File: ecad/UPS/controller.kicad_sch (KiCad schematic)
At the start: 32 parts, among them J2 Conn_01x05_Socket, SW1 SW_Push, SW2 SW_Push, U1 STM32L152RCT6, U2 AP2112K-3.3TRG1

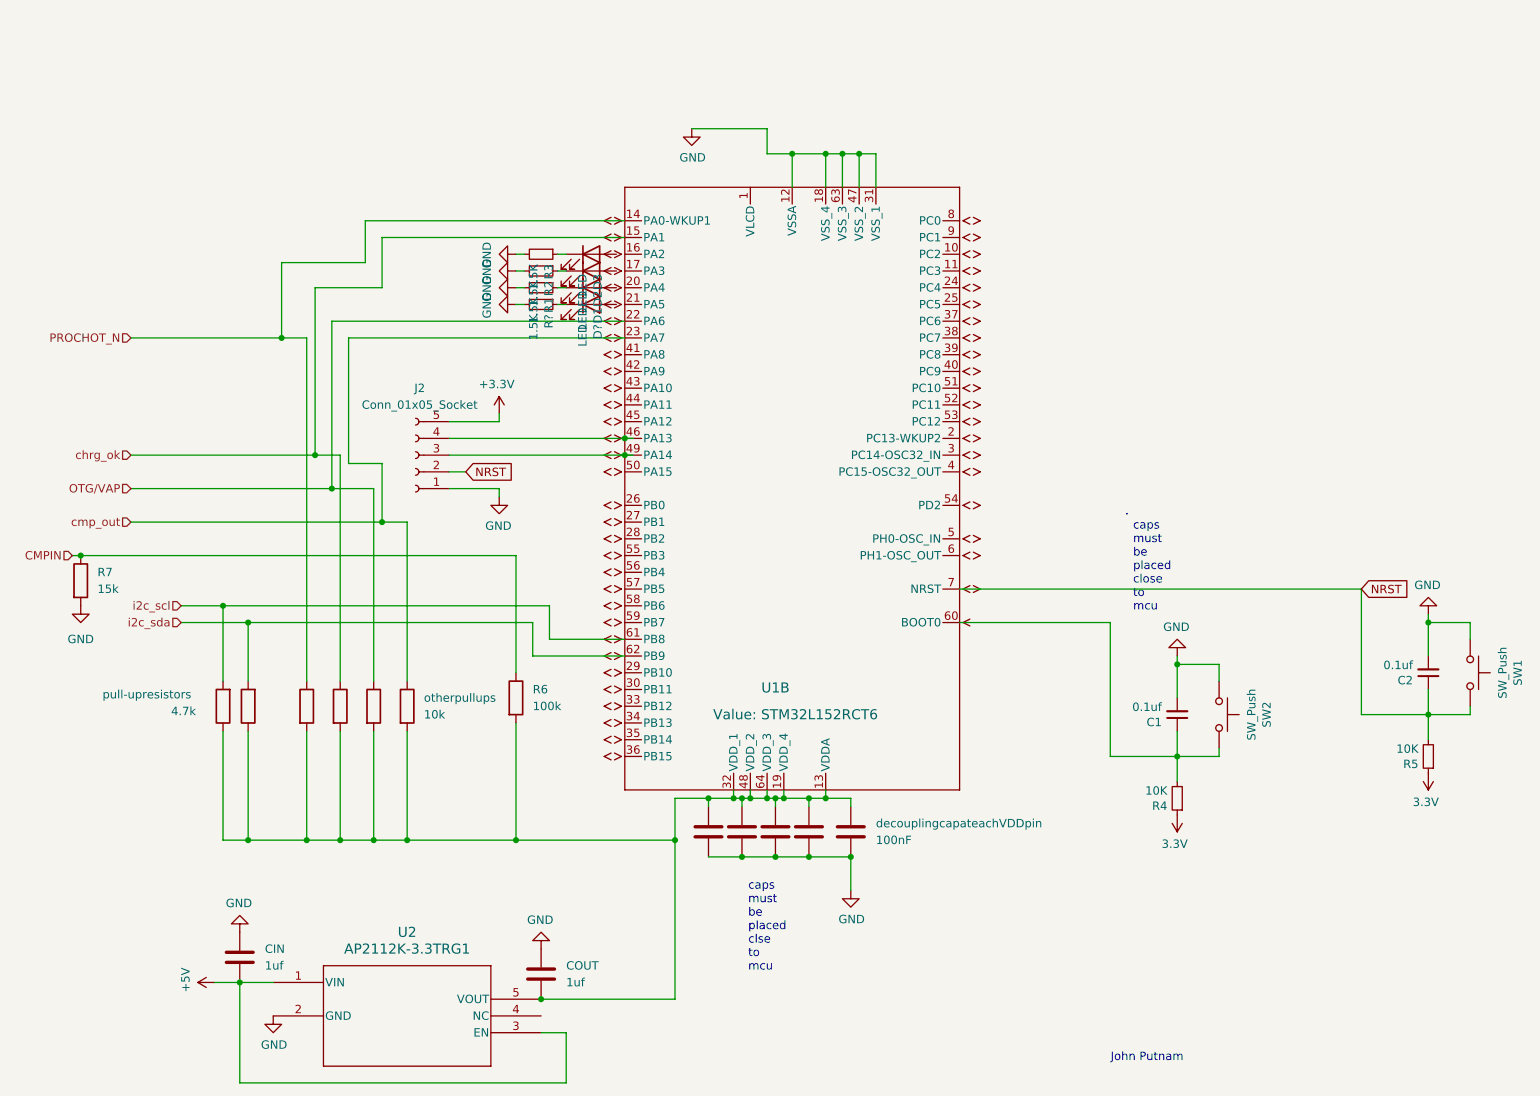
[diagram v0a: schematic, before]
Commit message: Made Power Net Class and set up board parameters and constraints
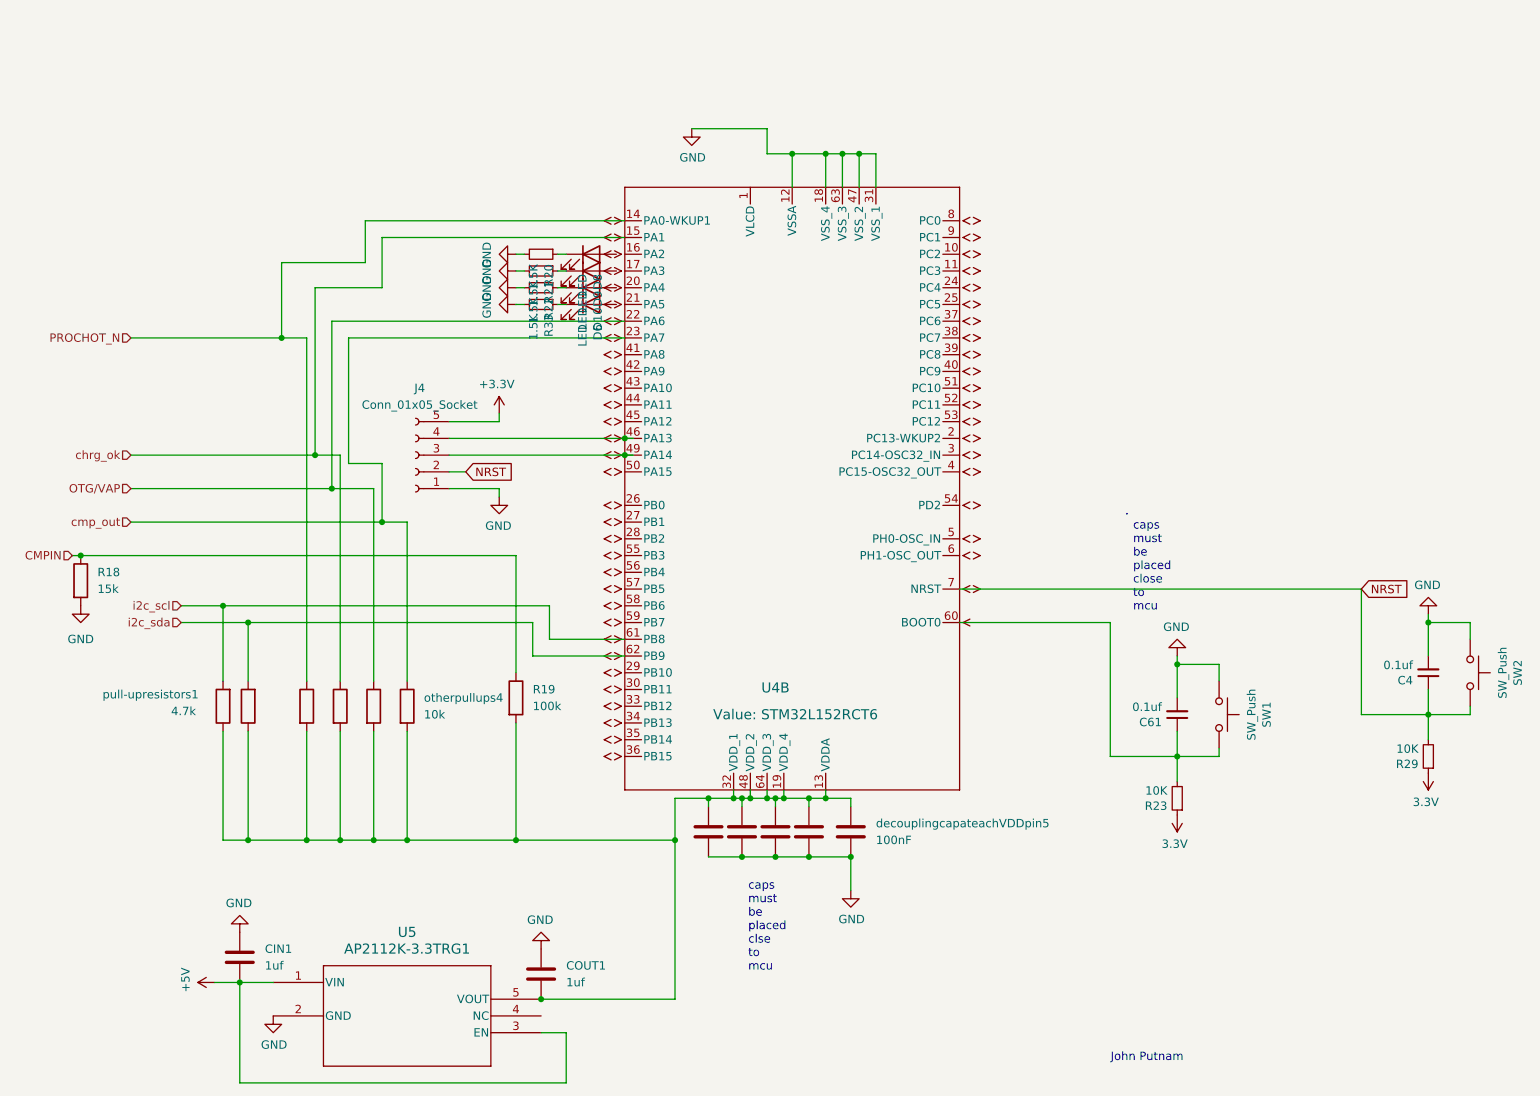
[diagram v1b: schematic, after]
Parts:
- gave numbers to parts that had none: 2
- renumbered C2 to C4, C1 to C61, CIN to CIN1, COUT to COUT1, D1 to D10, D3 to D8, D2 to D9, J2 to J4, R7 to R18, R6 to R19, R3 to R20, R2 to R21, R1 to R22, R4 to R23, R5 to R29, SW2 to SW1, SW1 to SW2, U1 to U4, U2 to U5, decouplingcapateachVDDpin4 to decouplingcapateachVDDpin1, decouplingcapateachVDDpin3 to decouplingcapateachVDDpin2, decouplingcapateachVDDpin2 to decouplingcapateachVDDpin3, decouplingcapateachVDDpin1 to decouplingcapateachVDDpin4, decouplingcapateachVDDpin to decouplingcapateachVDDpin5, otherpullups3 to otherpullups1, otherpullups1 to otherpullups3, otherpullups to otherpullups4, pull-upresistoronSDA to pull-upresistoronSDA1, pull-upresistors to pull-upresistors1

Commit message: Moved most components where they belong-ish
Barrel Jack's on the end as well as battery connector for now.  The MOSFET's need to be really close to the caps in the charger module
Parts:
- U4: footprint LQFP64-10x10mm -> UPS:LQFP64-10x10mm
- U5: footprint SOT_RG1_DIO -> UPS:SOT_RG1_DIO
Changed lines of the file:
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@@
 			)
 		)
-		(property "Footprint" "SOT_RG1_DIO"
+		(property "Footprint" "UPS:SOT_RG1_DIO"
 			(at 72.136 168.656 0)
 			(effects
@@
 			)
 		)
-		(property "Footprint" "LQFP64-10x10mm"
+		(property "Footprint" "UPS:LQFP64-10x10mm"
 			(at 119.888 22.606 0)
 			(effects
